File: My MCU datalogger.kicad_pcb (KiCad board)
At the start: 2 copper layers, 0 parts

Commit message: PCB Update
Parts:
- added U1: 24LC1025, Package_SO:SOIC-8_3.9x4.9mm_P1.27mm, F.Cu at (72.3, 59.7)
- added U2: DS1307Z, Silicon-Standard:SO08-TIGHT, F.Cu at (71.2, 66.8)
- added U3: 24LC1025, Package_SO:SOIC-8_3.9x4.9mm_P1.27mm, F.Cu at (80.7, 59.7)
- added U4: ATMEGA328P-AU, digikey-footprints:TQFP-32_7x7mm, F.Cu at (62.3, 62.2)
- added Y1: Crystal, Crystal:Crystal_SMD_5032-2Pin_5.0x3.2mm_HandSoldering, F.Cu at (61.7, 70.3)

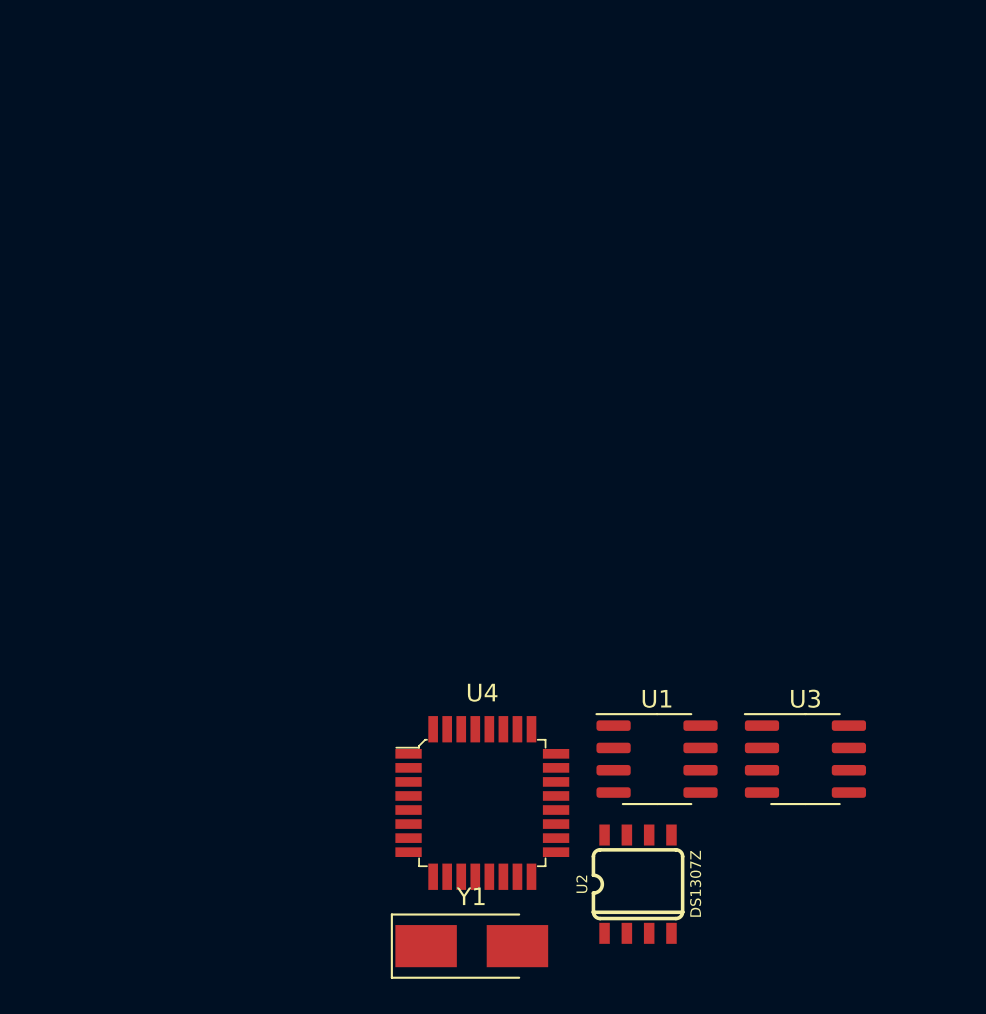
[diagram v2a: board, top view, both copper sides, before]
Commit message: Fixed ERC errors in schematic
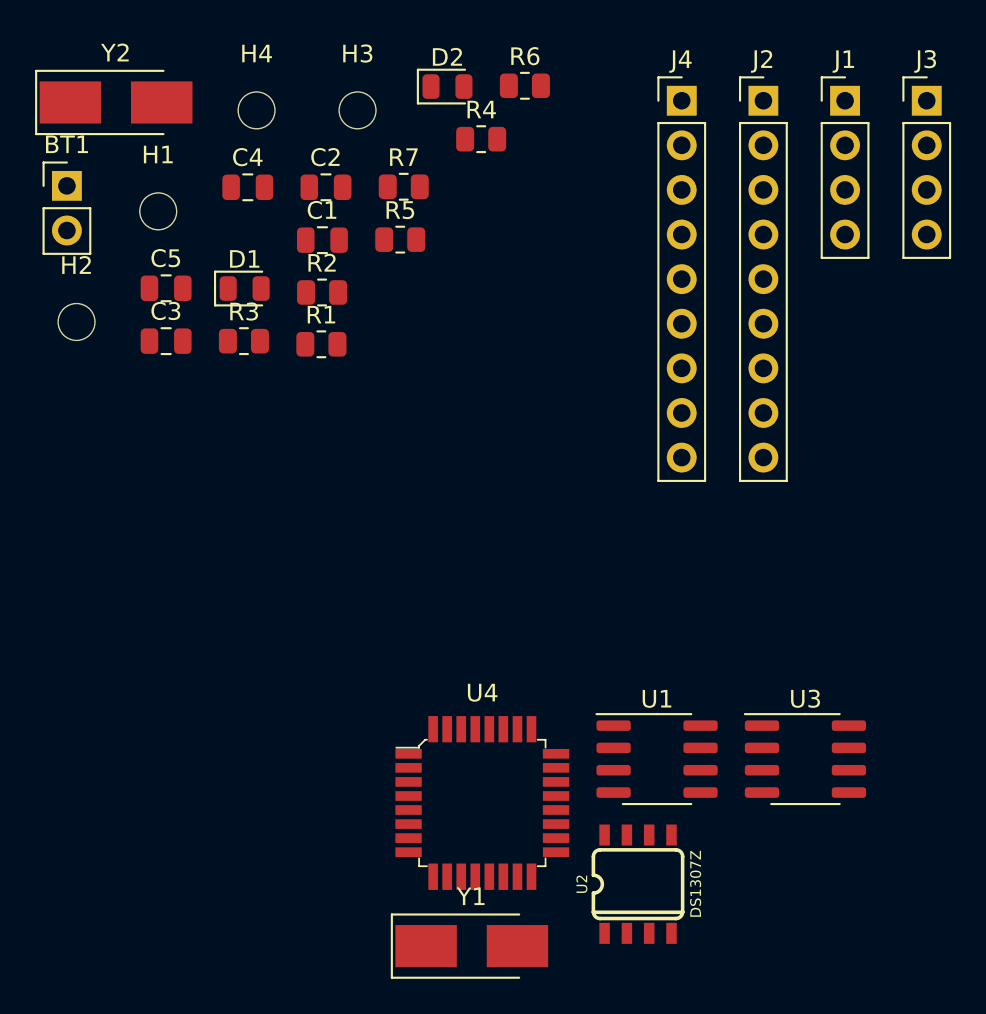
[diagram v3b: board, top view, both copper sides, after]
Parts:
- added BT1: Battery, Connector_PinHeader_2.54mm:PinHeader_1x02_P2.54mm_Vertical, F.Cu at (38.7, 27.0)
- added C1: 0,1uF, Capacitor_SMD:C_0805_2012Metric, F.Cu at (53.2, 30.1)
- added C2: 22pF, Capacitor_SMD:C_0805_2012Metric, F.Cu at (53.4, 27.1)
- added C3: 22pF, Capacitor_SMD:C_0805_2012Metric, F.Cu at (44.3, 35.9)
- added C4: 0.1uF, Capacitor_SMD:C_0805_2012Metric, F.Cu at (49.0, 27.1)
- added C5: 100nF, Capacitor_SMD:C_0805_2012Metric, F.Cu at (44.3, 32.9)
- added D1: LED, LED_SMD:LED_0805_2012Metric, F.Cu at (48.8, 32.9)
- added D2: LED, LED_SMD:LED_0805_2012Metric, F.Cu at (60.3, 21.4)
- added H1: MountingHole, MountingHole:MountingHole_2.1mm, F.Cu at (43.9, 28.5)
- added H2: MountingHole, MountingHole:MountingHole_2.1mm, F.Cu at (39.2, 34.8)
- added H3: MountingHole, MountingHole:MountingHole_2.1mm, F.Cu at (55.2, 22.7)
- added H4: MountingHole, MountingHole:MountingHole_2.1mm, F.Cu at (49.5, 22.7)
- added J1: Conn_01x04_Male, Connector_PinHeader_2.54mm:PinHeader_1x04_P2.54mm_Vertical, F.Cu at (83.0, 22.2)
- added J2: Conn_01x09_Male, Connector_PinHeader_2.54mm:PinHeader_1x09_P2.54mm_Vertical, F.Cu at (78.3, 22.2)
- added J3: Conn_01x04_Male, Connector_PinHeader_2.54mm:PinHeader_1x04_P2.54mm_Vertical, F.Cu at (87.6, 22.2)
- added J4: Conn_02x03_Odd_Even, Connector_PinHeader_2.54mm:PinHeader_1x09_P2.54mm_Vertical, F.Cu at (73.7, 22.2)
- added R1: 10K, Resistor_SMD:R_0805_2012Metric, F.Cu at (53.1, 36.1)
- added R2: 10K, Resistor_SMD:R_0805_2012Metric, F.Cu at (53.2, 33.1)
- added R3: 4.7K, Resistor_SMD:R_0805_2012Metric, F.Cu at (48.7, 35.9)
- added R4: 4.7K, Resistor_SMD:R_0805_2012Metric, F.Cu at (62.2, 24.4)
- added R5: 330, Resistor_SMD:R_0805_2012Metric, F.Cu at (57.6, 30.1)
- added R6: 10K, Resistor_SMD:R_0805_2012Metric, F.Cu at (64.7, 21.3)
- added R7: 330, Resistor_SMD:R_0805_2012Metric, F.Cu at (57.8, 27.1)
- added Y2: 16 MHz, Crystal:Crystal_SMD_5032-2Pin_5.0x3.2mm_HandSoldering, F.Cu at (41.5, 22.3)
- Y1: value Crystal -> 32.768 KHz

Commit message: Verification
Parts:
- J4: footprint Connector_PinHeader_2.54mm:PinHeader_1x09_P2.54mm_Vertical -> Connector_PinHeader_2.54mm:PinHeader_2x03_P2.54mm_Vertical
- moved J4 7.59 mm to (69.7, 28.6)
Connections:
- net /Connectors/D8 renamed /D8
- BT1 pad 1: Net-(BT1-Pad1) -> /Vcc
- C1 pad 1: /VCC -> /Vcc
- C5 pad 1: Net-(BT1-Pad1) -> /Vcc
- D2 pad 2: Net-(BT1-Pad1) -> /Vcc
- J1 pad 3: /Connectors/SDA -> /SDA
- J1 pad 4: /Connectors/SCK -> /SCK
- J2 pad 1: /Connectors/D2 -> /D2
- J2 pad 2: /Connectors/D3 -> /D3
- J2 pad 3: /Connectors/D4 -> /D4
- J2 pad 4: /Connectors/D5 -> /D5
- J2 pad 5: /Connectors/D6 -> /D6
- J2 pad 6: /Connectors/D7 -> /D7
- J3 pad 3: /Connectors/RX -> /RX
- J3 pad 4: /Connectors/TX -> /TX
- J4 pad 1: /Connectors/MISO -> /MISO
- J4 pad 3: /Connectors/SCK -> /SCK
- J4 pad 4: /Connectors/MOSI -> /MOSI
- J4 pad 5: /Connectors/RESET -> /RESET
- R1 pad 1: /VCC -> /Vcc
- R2 pad 1: /VCC -> /Vcc
- R3 pad 1: /VCC -> /Vcc
- R4 pad 1: /VCC -> /Vcc
- R6 pad 1: /VCC -> /Vcc
- U1 pad 1: /VCC -> /Vcc
- U1 pad 2: /VCC -> /Vcc
- U1 pad 3: /VCC -> /Vcc
- U1 pad 8: /VCC -> /Vcc
- U2 pad 8: /VCC -> /Vcc
- U3 pad 1: /VCC -> /Vcc
- U3 pad 3: /VCC -> /Vcc
- U3 pad 8: /VCC -> /Vcc
- U4 pad 18: Net-(BT1-Pad1) -> /Vcc
- U4 pad 3: unconnected-(U4-Pad3) -> GND
- U4 pad 4: Net-(BT1-Pad1) -> /Vcc
